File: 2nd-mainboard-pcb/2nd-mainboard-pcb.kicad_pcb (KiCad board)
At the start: 2 copper layers, 36.9 x 36.8 mm, 124 parts, among them J1 PJ-082BH, J10 Servo Motor BL Touch, J11 T3, J12 Steckverbinder_Male_Fans, J13 Steckverbinder_Female_Leistung, J14 Steckverbinder_Male_Leistung, J15 Steckverbinder_Female_Motoren, J16 ISP, J18 Quartz, J19 T2, J2 Fan_12/5V_Regelung, J20 T2, J21 T2, J22 T3, J23 Conn_01x04_Socket, J3 FAN0, J4 FAN1, J5 FAN2, J6 FAN3, J7 Stepper Motor, J8 Servo Motor SM, J9 Microstepping, P1 USB_C_Plug_USB2.0, U1 SQJ409EP-T1_GE3, U10 ATmega328PB-A, U12 MPU-6050, U2 SZ1SMB5927BT3G, U3 TPS56837HRPAR, U4 TPS565208, U5 FT232RL, U6 PTS647SM38SMTR2LFS, U7 TPM16050-S6TR, U8 RJK0456DPB-00-J5, U9 RJK0456DPB-00-J5, Y1 ECS-160-18-4X-CKM

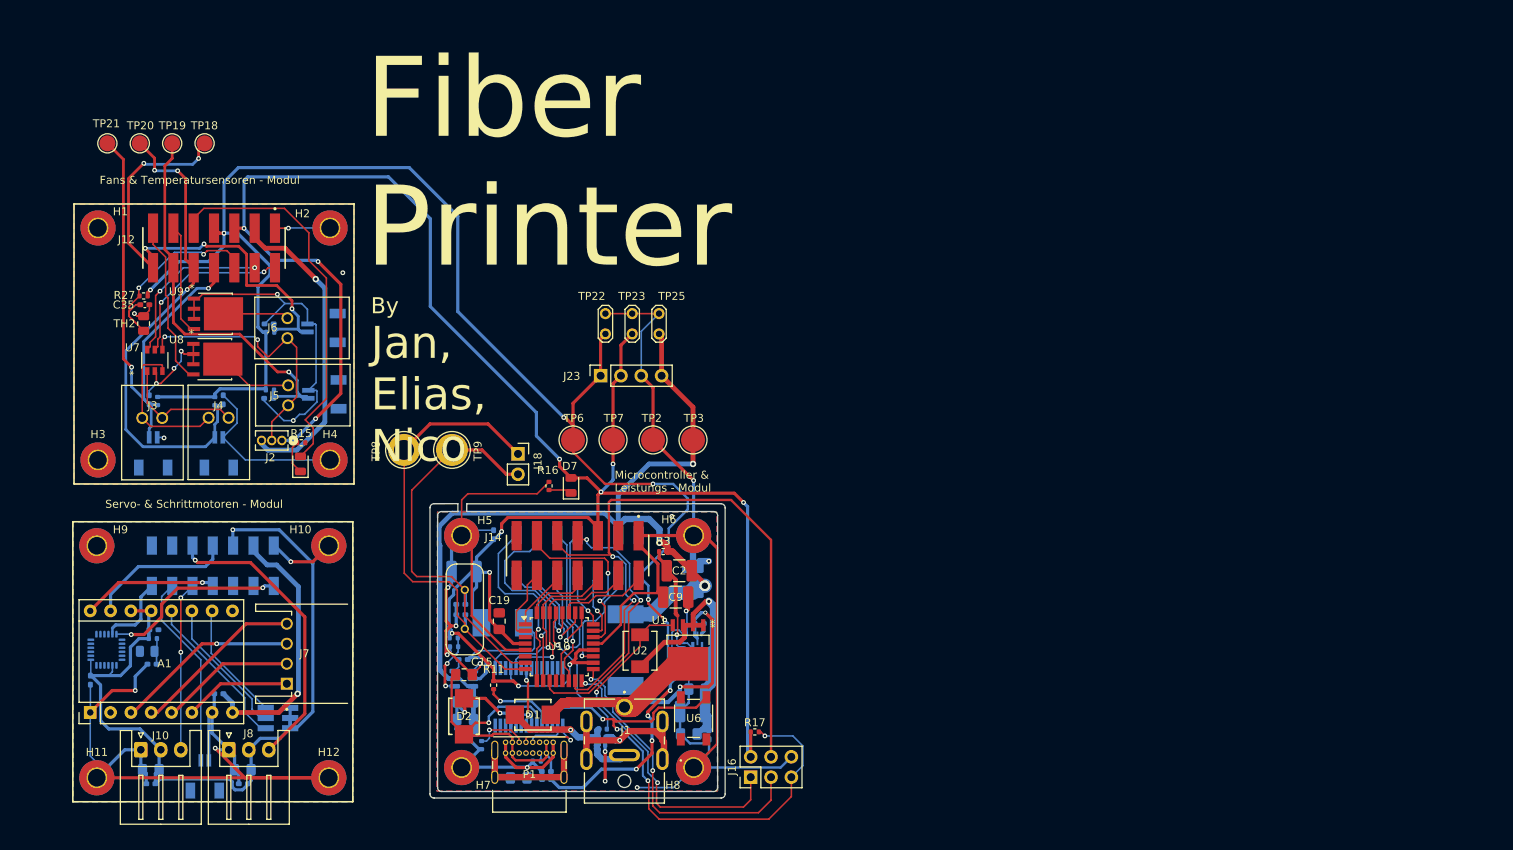
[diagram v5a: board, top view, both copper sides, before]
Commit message: umriss grob zum funktinoieren gebracht
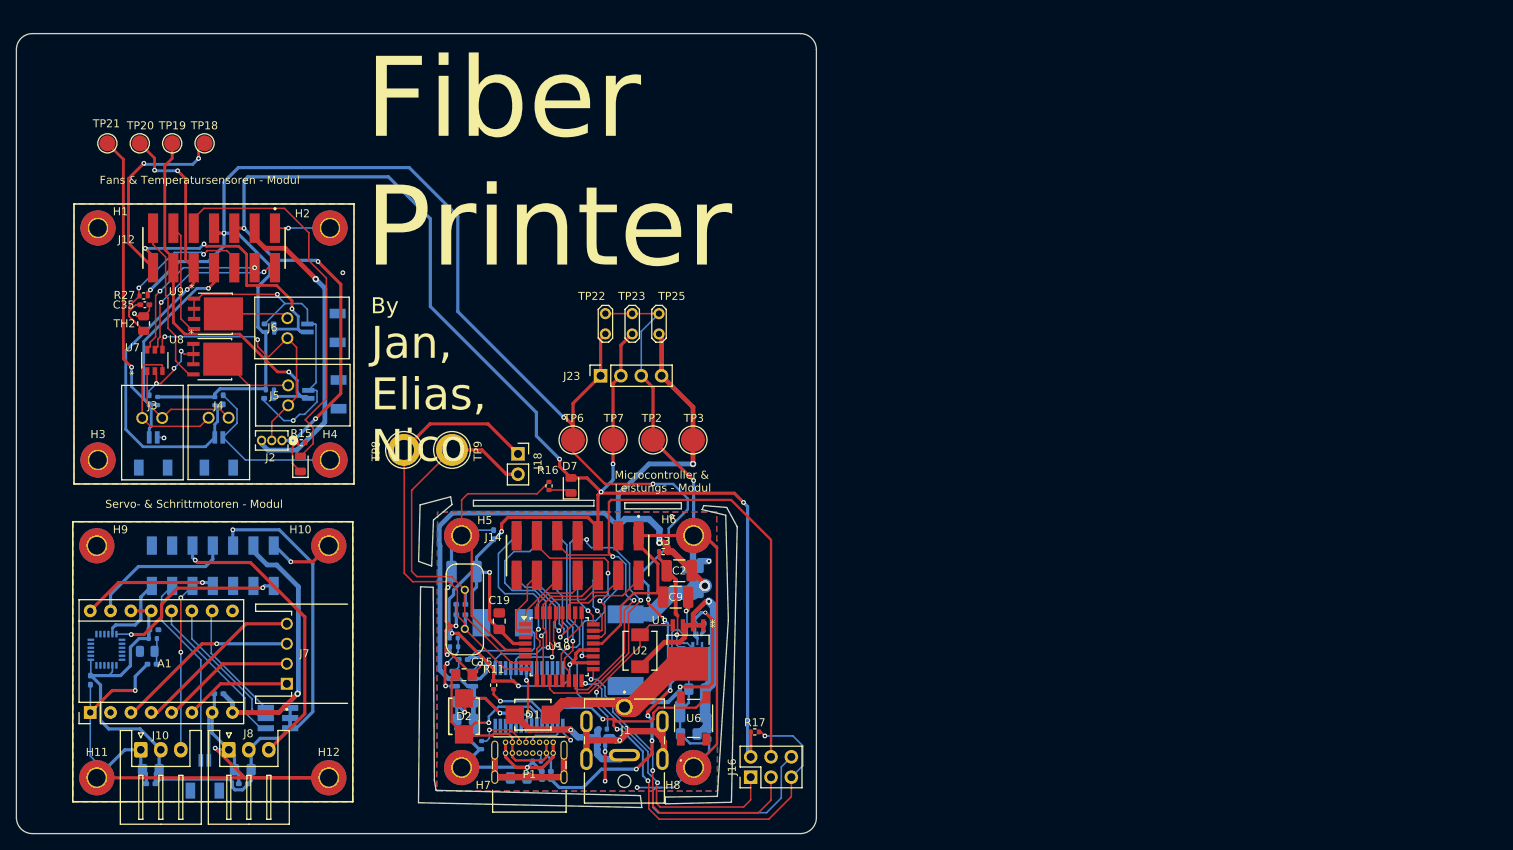
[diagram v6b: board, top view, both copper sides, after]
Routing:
- net GND: track 477.9 -> 491.2 mm
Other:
- board size 36.9 x 36.8 mm -> 100 x 100 mm

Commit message: layout: bahnenbreiten bearbeitet, neu geroutet bei 12V Buck, Bauteile teilweise ausgetauscht
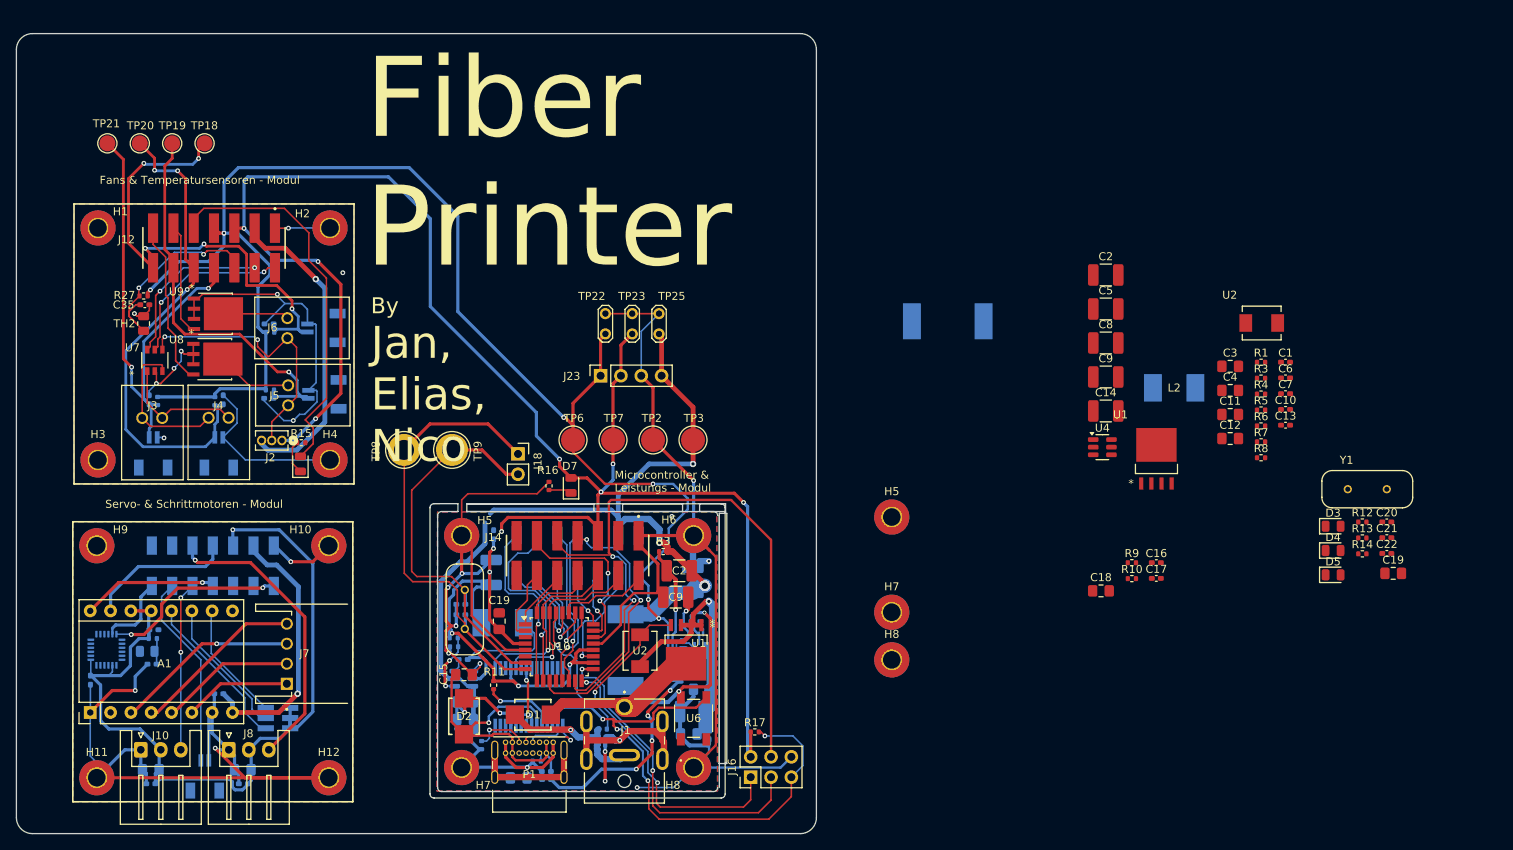
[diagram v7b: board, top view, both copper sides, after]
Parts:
- added C1: 100nF, Capacitor_SMD:C_0402_1005Metric_Pad0.74x0.62mm_HandSolder, F.Cu at (208.6, 91.1)
- added C10: 100nF, Capacitor_SMD:C_0402_1005Metric_Pad0.74x0.62mm_HandSolder, F.Cu at (208.6, 97.0)
- added C11: 10µF, Capacitor_SMD:C_0805_2012Metric_Pad1.18x1.45mm_HandSolder, F.Cu at (201.7, 97.6)
- added C12: 10µF, Capacitor_SMD:C_0805_2012Metric_Pad1.18x1.45mm_HandSolder, F.Cu at (201.7, 100.6)
- added C13: 100nF, Capacitor_SMD:C_0402_1005Metric_Pad0.74x0.62mm_HandSolder, F.Cu at (208.6, 99.0)
- added C14: 22µF, Capacitor_SMD:C_1210_3225Metric_Pad1.33x2.70mm_HandSolder, F.Cu at (186.2, 97.2)
- added C16: 100nF, Capacitor_SMD:C_0402_1005Metric_Pad0.74x0.62mm_HandSolder, F.Cu at (192.5, 116.1)
- added C17: 100nF, Capacitor_SMD:C_0402_1005Metric_Pad0.74x0.62mm_HandSolder, F.Cu at (192.5, 118.1)
- added C18: 1uF, Capacitor_SMD:C_0805_2012Metric_Pad1.18x1.45mm_HandSolder, F.Cu at (185.6, 119.7)
- added C19: 4.7uF, Capacitor_SMD:C_0805_2012Metric_Pad1.18x1.45mm_HandSolder, F.Cu at (222.1, 117.5)
- added C2: 22nF, Capacitor_SMD:C_1210_3225Metric_Pad1.33x2.70mm_HandSolder, F.Cu at (186.2, 80.2)
- added C20: 100nF, Capacitor_SMD:C_0402_1005Metric_Pad0.74x0.62mm_HandSolder, F.Cu at (221.3, 111.0)
- added C21: 18pF, Capacitor_SMD:C_0402_1005Metric_Pad0.74x0.62mm_HandSolder, F.Cu at (221.3, 113.0)
- added C22: 18pF, Capacitor_SMD:C_0402_1005Metric_Pad0.74x0.62mm_HandSolder, F.Cu at (221.3, 115.0)
- added C3: 10µF, Capacitor_SMD:C_0805_2012Metric_Pad1.18x1.45mm_HandSolder, F.Cu at (201.7, 91.6)
- added C4: 10µF, Capacitor_SMD:C_0805_2012Metric_Pad1.18x1.45mm_HandSolder, F.Cu at (201.7, 94.6)
- added C5: 10µF, Capacitor_SMD:C_1210_3225Metric_Pad1.33x2.70mm_HandSolder, F.Cu at (186.2, 84.4)
- added C6: 100nF, Capacitor_SMD:C_0402_1005Metric_Pad0.74x0.62mm_HandSolder, F.Cu at (208.6, 93.0)
- added C7: 100nF, Capacitor_SMD:C_0402_1005Metric_Pad0.74x0.62mm_HandSolder, F.Cu at (208.6, 95.0)
- added C8: 47µF, Capacitor_SMD:C_1210_3225Metric_Pad1.33x2.70mm_HandSolder, F.Cu at (186.2, 88.7)
- added C9: 22nF, Capacitor_SMD:C_1210_3225Metric_Pad1.33x2.70mm_HandSolder, F.Cu at (186.2, 92.9)
- added D3: YELLOW, LED_SMD:LED_0805_2012Metric, F.Cu at (214.6, 111.6)
- added D4: YELLOW, LED_SMD:LED_0805_2012Metric, F.Cu at (214.6, 114.6)
- added D5: YELLOW, LED_SMD:LED_0805_2012Metric, F.Cu at (214.6, 117.7)
- added H5: MountHole, MountingHole:MountingHole_2.2mm_M2_Pad_TopBottom, F.Cu at (159.4, 110.4)
- added H7: MountHole, MountingHole:MountingHole_2.2mm_M2_Pad_TopBottom, F.Cu at (159.4, 122.3)
- added H8: MountHole, MountingHole:MountingHole_2.2mm_M2_Pad_TopBottom, F.Cu at (159.4, 128.3)
- added L1: 4.7µH, Imported_Component_Footprints:SPM10040T_4R7M_HZ, B.Cu at (166.4, 86.0)
- added L2: 3.3µH, Imported_Component_Footprints:IHLP2525CZER3R3M11, B.Cu at (194.7, 94.3)
- added R1: 100k, Resistor_SMD:R_0402_1005Metric, F.Cu at (205.6, 91.1)
- added R10: 5k1, Resistor_SMD:R_0402_1005Metric, F.Cu at (189.4, 118.1)
- added R12: 330, Resistor_SMD:R_0402_1005Metric, F.Cu at (218.2, 111.0)
- added R13: 330, Resistor_SMD:R_0402_1005Metric, F.Cu at (218.2, 113.0)
- added R14: 330, Resistor_SMD:R_0402_1005Metric, F.Cu at (218.2, 115.0)
- added R3: 30k, Resistor_SMD:R_0402_1005Metric, F.Cu at (205.6, 93.1)
- added R4: 1k58, Resistor_SMD:R_0402_1005Metric, F.Cu at (205.6, 95.1)
- added R5: 30.1k, Resistor_SMD:R_0402_1005Metric, F.Cu at (205.6, 97.0)
- added R6: 10, Resistor_SMD:R_0402_1005Metric, F.Cu at (205.6, 99.0)
- added R7: 54.9k, Resistor_SMD:R_0402_1005Metric, F.Cu at (205.6, 101.0)
- added R8: 10k, Resistor_SMD:R_0402_1005Metric, F.Cu at (205.6, 103.0)
- added R9: 5k1, Resistor_SMD:R_0402_1005Metric, F.Cu at (189.4, 116.1)
- added U1: SQJ409EP-T1_GE3, Imported_Component_Footprints:SQJ409EP_T1_GE3, F.Cu at (192.5, 102.6)
- added U2: SZ1SMB5927BT3G, Imported_Component_Footprints:SZ1SMB5927BT3G, F.Cu at (205.7, 86.2)
- added U4: TPS565208, Package_TO_SOT_SMD:SOT-23-6, F.Cu at (185.7, 101.7)
- added Y1: ECS-160-18-4X-CKM, Imported_Component_Footprints:XTAL_ECS-160-18-4X-CKM, F.Cu at (218.9, 107.0)
- R2: footprint Resistor_SMD:R_0402_1005Metric -> Resistor_SMD:R_0603_1608Metric
- moved C14 3.40 mm to (109.3, 117.4), turned to 90 degrees
- moved C3 0.59 mm to (135.7, 132.0)
- moved C1 0.48 mm to (134.9, 123.5)
- moved R4 0.46 mm to (134.2, 129.9)
- moved R5 0.40 mm to (135.2, 129.9)
- moved R2 0.37 mm to (132.9, 130.0)
- moved U1 0.24 mm to (133.7, 127.5)
- moved U3 0.21 mm to (135.0, 126.4)
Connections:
- C15 pad 1: +5V_USBC -> AREF
- D2 pad 2: +5V_USBC -> AREF
- P1 pad A1: (no net) -> GND
- P1 pad A12: (no net) -> GND
- P1 pad A4: (no net) -> AREF
- P1 pad A5: (no net) -> Net-(P1-CC)
- P1 pad A6: (no net) -> USBD+
- P1 pad A7: (no net) -> USBD-
- P1 pad A9: (no net) -> AREF
- P1 pad B1: (no net) -> GND
- P1 pad B12: (no net) -> GND
- P1 pad B4: (no net) -> AREF
- P1 pad B5: (no net) -> Net-(P1-VCONN)
- P1 pad B9: (no net) -> AREF
- P1 pad S1: (no net) -> Net-(P1-SHIELD)
- R11 pad 1: AREF -> +5V_POW
- R2 pad 1: +5V_USBC -> AREF
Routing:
- net AREF: track 360.1 -> 344.9 mm
- net +5V_POW: track 196.5 -> 211.2 mm, vias 7 -> 8
- net GND: track 491.2 -> 478.2 mm, vias 27 -> 28
- net Net-(U3-FB): track 17.2 -> 22.6 mm
- net +12V: track 189.4 -> 186.5 mm
- net Net-(U3-PG): track 6.96 -> 4.44 mm
- net SCK: track 39.5 -> 41.7 mm
- net FAN_2_PWM: track 44.4 -> 43.1 mm
- net FAN_3_PWM: track 39.0 -> 38.3 mm
- net +5V_USBC: track 81.3 -> 81.9 mm
- net RESET: track 99.4 -> 99.9 mm
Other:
- outline, holes or cut-outs redrawn

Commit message: pcb ausschnitt bearbeitet
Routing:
- net GND: track 478.2 -> 489.7 mm
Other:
- outline, holes or cut-outs redrawn
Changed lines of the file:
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@@
-	)
-	(gr_line
-		(start 106.29 108.78)
-		(end 138.09 108.77)
-		(stroke
-			(width 0.05)
-			(type default)
-		)
-		(layer "Edge.Cuts")
-	)
-	(gr_arc
-		(start 102.2 145.55)
-		(mid 101.846447 145.403553)
-		(end 101.7 145.05)
-		(stroke
-			(width 0.05)
-			(type default)
-		)
-		(layer "Edge.Cuts")
 	)
 	(gr_line
@@
 		(layer "Edge.Cuts")
 	)
-	(gr_arc
-		(start 138.59 145.05)
-		(mid 138.443553 145.403553)
-		(end 138.09 145.55)
-		(stroke
-			(width 0.05)
-			(type default)
-		)
-		(layer "Edge.Cuts")
-	)
-	(gr_line
-		(start 102.6525 144.2425)
-		(end 102.6525 110.2425)
-		(stroke
-			(width 0.05)
-			(type default)
-		)
-		(layer "Edge.Cuts")
-	)
-	(gr_line
-		(start 138.59 109.27)
-		(end 138.59 145.05)
-		(stroke
-			(width 0.05)
-			(type default)
-		)
-		(layer "Edge.Cuts")
-	)
-	(gr_line
-		(start 137.1525 144.7425)
-		(end 103.1525 144.7425)
-		(stroke
-			(width 0.05)
-			(type default)
-		)
-		(layer "Edge.Cuts")
-	)
-	(gr_arc
-		(start 103.1525 144.7425)
-		(mid 102.798947 144.596053)
-		(end 102.6525 144.2425)
-		(stroke
-			(width 0.05)
-			(type default)
-		)
-		(layer "Edge.Cuts")
-	)
 	(gr_rect
 		(start 106.3 108.775)
@@
 		(layer "Edge.Cuts")
 	)
-	(gr_arc
-		(start 102.6525 110.2425)
-		(mid 102.798947 109.888947)
-		(end 103.1525 109.7425)
+	(gr_rect
+		(start 130.5 144.7425)
+		(end 138.8225 145.56)
 		(stroke
 			(width 0.05)
 			(type default)
 		)
+		(fill none)
 		(layer "Edge.Cuts")
 	)
 	(gr_rect
 		(start 137.860001 109.9625)
-		(end 138.797501 141.24)
+		(end 138.797501 144.58)
 		(stroke
 			(width 0.05)
@@
 		(layer "Edge.Cuts")
 	)
-	(gr_arc
-		(start 138.09 108.77)
-		(mid 138.443553 108.916447)
-		(end 138.59 109.27)
+	(gr_rect
+		(start 101.7 108.76)
+		(end 105.19 109.74)
 		(stroke
 			(width 0.05)
 			(type default)
 		)
-		(layer "Edge.Cuts")
-	)
-	(gr_line
-		(start 102.22 108.77)
-		(end 105.19 108.76)
-		(stroke
-			(width 0.05)
-			(type default)
-		)
+		(fill none)
 		(layer "Edge.Cuts")
 	)
@@
 		(layer "Edge.Cuts")
 	)
-	(gr_line
-		(start 106.3 109.7425)
-		(end 137.1525 109.7425)
+	(gr_rect
+		(start 101.69 118.75)
+		(end 102.6525 144.6125)
 		(stroke
 			(width 0.05)
 			(type default)
 		)
+		(fill none)
 		(layer "Edge.Cuts")
 	)
-	(gr_arc
-		(start 137.6525 144.2425)
-		(mid 137.506053 144.596053)
-		(end 137.1525 144.7425)
+	(gr_rect
+		(start 101.69 109.9625)
+		(end 102.6525 117.52)
 		(stroke
 			(width 0.05)
 			(type default)
 		)
+		(fill none)
 		(layer "Edge.Cuts")
 	)
-	(gr_arc
-		(start 101.7 109.27)
-		(mid 101.846447 108.916447)
-		(end 102.2 108.77)
+	(gr_rect
+		(start 101.6825 144.7425)
+		(end 128.61 145.54)
 		(stroke
 			(width 0.05)
 			(type default)
 		)
-		(layer "Edge.Cuts")
-	)
-	(gr_line
-		(start 105.19 109.74)
-		(end 105.19 108.76)
-		(stroke
-			(width 0.05)
-			(type default)
-		)
-		(layer "Edge.Cuts")
-	)
-	(gr_line
-		(start 138.09 145.55)
-		(end 102.2 145.55)
-		(stroke
-			(width 0.05)
-			(type default)
-		)
-		(layer "Edge.Cuts")
-	)
-	(gr_line
-		(start 101.7 145.05)
-		(end 101.7 109.27)
-		(stroke
-			(width 0.05)
-			(type default)
-		)
-		(layer "Edge.Cuts")
-	)
-	(gr_arc
-		(start 137.1525 109.7425)
-		(mid 137.506053 109.888947)
-		(end 137.6525 110.2425)
-		(stroke
-			(width 0.05)
-			(type default)
-		)
+		(fill none)
 		(layer "Edge.Cuts")
 	)
@@
 		(stroke
 			(width 0.1)
-			(type default)
-		)
-		(layer "Edge.Cuts")
-	)
-	(gr_line
-		(start 103.1525 109.7425)
-		(end 105.19 109.74)
-		(stroke
-			(width 0.05)
 			(type default)
 		)
@@
 	)
 	(segment
+		(start 129.57 144.2425)
+		(end 127.592702 144.2425)
+		(width 0.2)
+		(layer "B.Cu")
+		(net 1)
+	)
+	(segment
 		(start 114.4025 135.3125)
 		(end 114.225004 135.135004)
@@
 		(end 115.5193 143.0425)
 		(width 0.4)
+		(layer "B.Cu")
+		(net 1)
+	)
+	(segment
+		(start 130.1 147.16)
+		(end 142.86 147.16)
+		(width 0.2)
 		(layer "B.Cu")
 		(net 1)
@@
 	)
 	(segment
+		(start 129.57 144.2425)
+		(end 129.57 146.63)
+		(width 0.2)
+		(layer "B.Cu")
+		(net 1)
+	)
+	(segment
 		(start 136.585 139.81)
 		(end 134.6525 141.7425)
@@
 	)
 	(segment
-		(start 146.87 140.405012)
-		(end 145.532512 141.7425)
-		(width 0.3)
-		(layer "B.Cu")
-		(net 1)
-	)
-	(segment
 		(start 63.55265 139.519261)
 		(end 60.05265 143.019261)
@@
 		(end 74.47015 137.436761)
 		(width 0.4)
+		(layer "B.Cu")
+		(net 1)
+	)
+	(segment
+		(start 132.1525 144.2425)
+		(end 129.57 144.2425)
+		(width 0.2)
 		(layer "B.Cu")
 		(net 1)
@@
 	)
 	(segment
-		(start 145.532512 141.7425)
-		(end 134.6525 141.7425)
-		(width 0.3)
-		(layer "B.Cu")
-		(net 1)
-	)
-	(segment
 		(start 85.392938 97.59315)
 		(end 84.613448 98.37264)
@@
 	)
 	(segment
+		(start 145.61 144.41)
+		(end 145.61 141.665012)
+		(width 0.2)
+		(layer "B.Cu")
+		(net 1)
+	)
+	(segment
 		(start 60.05265 141.119261)
 		(end 59.23015 140.296761)
@@
 	)
 	(segment
+		(start 145.61 141.665012)
+		(end 146.87 140.405012)
+		(width 0.2)
+		(layer "B.Cu")
+		(net 1)
+	)
+	(segment
 		(start 67.60185 100.47315)
 		(end 68.38185 100.47315)
@@
 		(end 74.85265 139.319261)
 		(width 0.4)
+		(layer "B.Cu")
+		(net 1)
+	)
+	(segment
+		(start 142.86 147.16)
+		(end 145.61 144.41)
+		(width 0.2)
 		(layer "B.Cu")
 		(net 1)
@@
 	)
 	(segment
+		(start 129.57 146.63)
+		(end 130.1 147.16)
+		(width 0.2)
+		(layer "B.Cu")
+		(net 1)
+	)
+	(segment
 		(start 86.38185 84.47315)
 		(end 86.38185 86.29315)
@@
 		(width 0.2)
 		(layer "B.Cu")
-		(net 1)
-	)
-	(segment
-		(start 132.1525 144.2425)
-		(end 127.592702 144.2425)
-		(width 0.2)
-		(layer "B.Cu")
